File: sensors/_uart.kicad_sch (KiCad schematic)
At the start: 19 parts, among them J5 JP_GPS, J6 JP_RADIO, U1 SC16IS752IPW

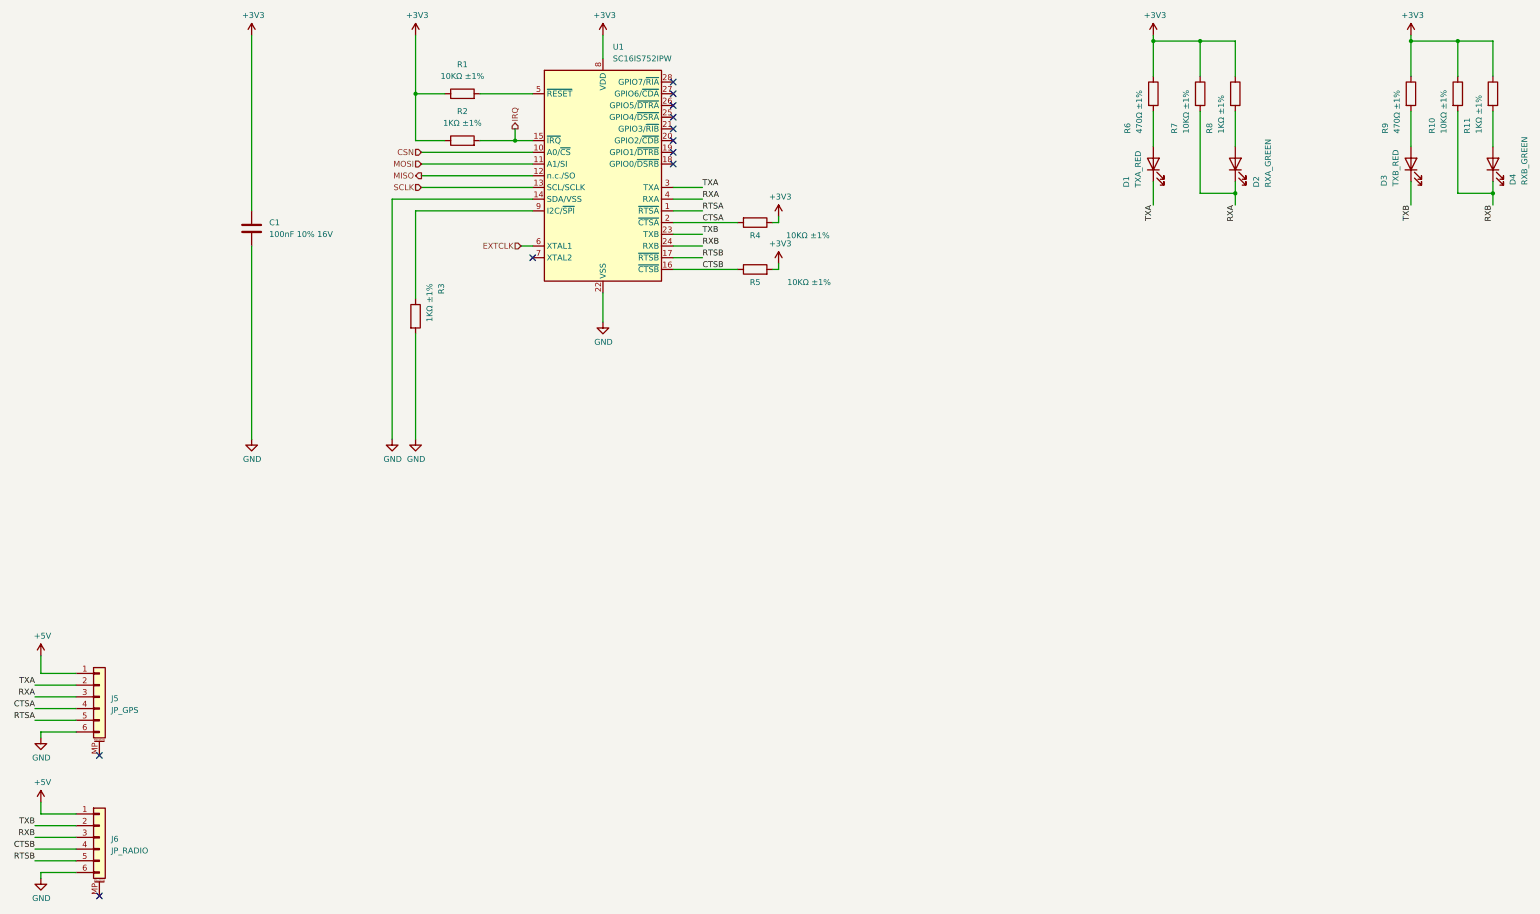
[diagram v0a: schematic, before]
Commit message: changes from dshot branch
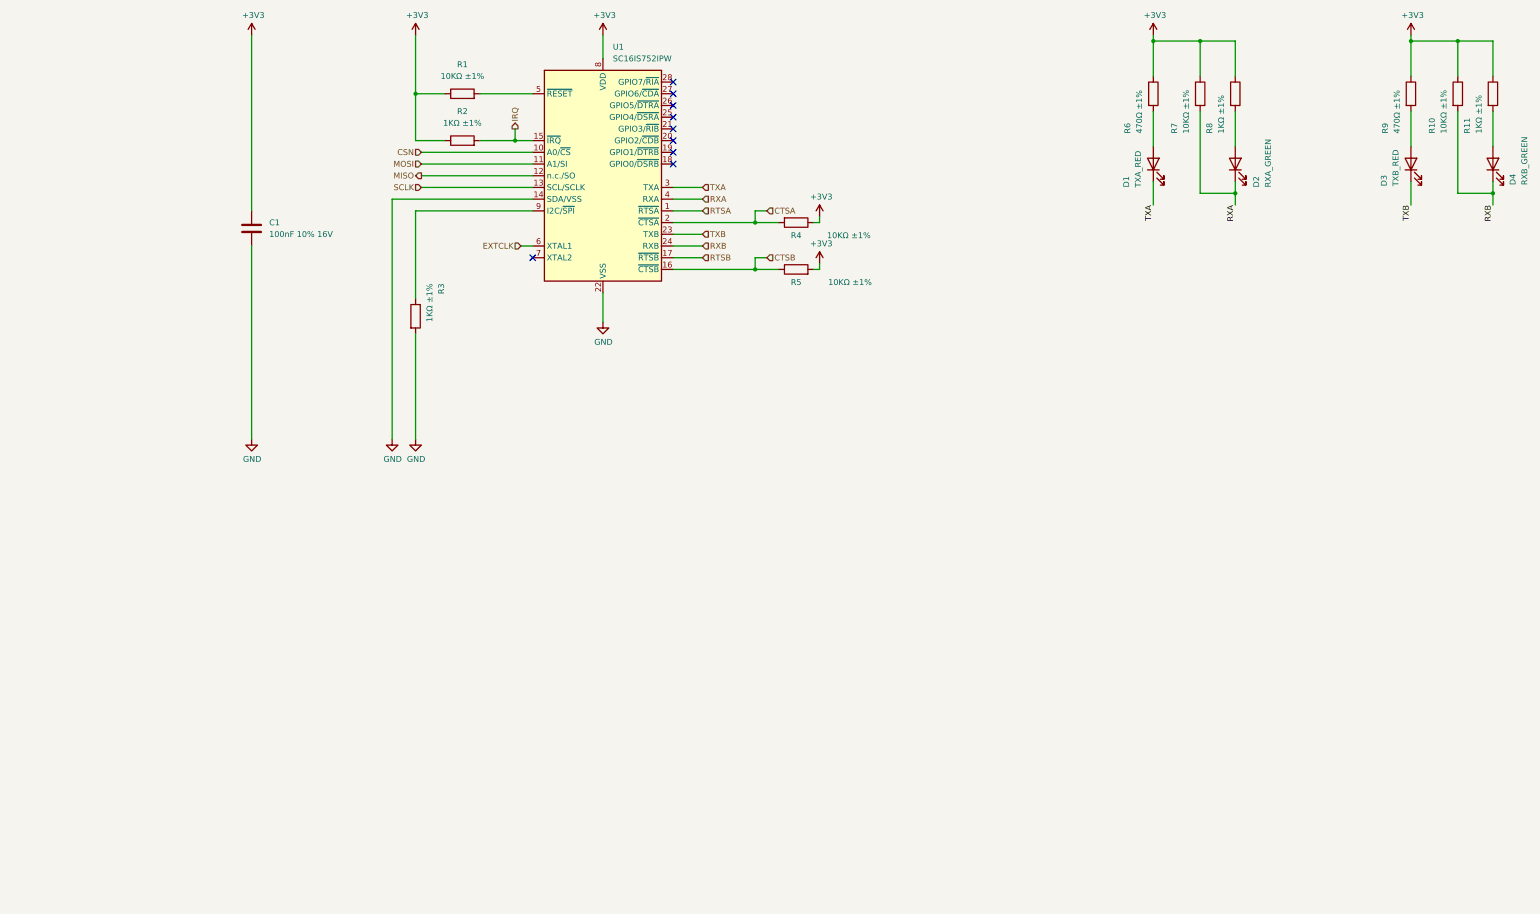
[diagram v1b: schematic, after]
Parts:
- removed J5: JP_GPS, Connector_Molex:Molex_PicoBlade_53261-0671_1x06-1MP_P1.25mm_Horizontal, symbol Connector_Generic_MountingPin:Conn_01x06_MountingPin
- removed J6: JP_RADIO, Connector_Molex:Molex_PicoBlade_53261-0671_1x06-1MP_P1.25mm_Horizontal, symbol Connector_Generic_MountingPin:Conn_01x06_MountingPin
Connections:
- no-connect marks 11 -> 9
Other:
- moved on the sheet: R4, R5

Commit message: replace MS561101 pressure sensor with SPL06-001
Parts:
- C1: Part CC0402X7R50V104KN -> CL05B104KB54PNC
- R11, R2, R3, R8: Part SCR0402F1K -> 0402WGF1001TCE
- R6, R9: Part FRC0402F4700TS -> 0402WGF4700TCE
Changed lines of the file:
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@@
 			)
 		)
-		(property "Part" "FRC0402F4700TS"
+		(property "Part" "0402WGF4700TCE"
 			(at 271.78 81.28 0)
 			(hide yes)
@@
 			)
 		)
-		(property "Part" "SCR0402F1K"
+		(property "Part" "0402WGF1001TCE"
 			(at 121.92 91.44 0)
 			(hide yes)
@@
 			)
 		)
-		(property "Part" "SCR0402F1K"
+		(property "Part" "0402WGF1001TCE"
 			(at 111.76 129.54 0)
 			(hide yes)
@@
 			)
 		)
-		(property "Part" "CC0402X7R50V104KN"
+		(property "Part" "CL05B104KB54PNC"
 			(at 76.2 110.49 0)
 			(hide yes)
@@
 			)
 		)
-		(property "Part" "SCR0402F1K"
+		(property "Part" "0402WGF1001TCE"
 			(at 345.44 81.28 0)
 			(hide yes)
@@
 			)
 		)
-		(property "Part" "SCR0402F1K"
+		(property "Part" "0402WGF1001TCE"
 			(at 289.56 81.28 0)
 			(hide yes)
@@
 			)
 		)
-		(property "Part" "FRC0402F4700TS"
+		(property "Part" "0402WGF4700TCE"
 			(at 327.66 81.28 0)
 			(hide yes)

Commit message: move SP3485 to sensors board and connect to UART port A
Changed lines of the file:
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@@
 	)
 	(hierarchical_label "RTSA"
-		(shape input)
+		(shape output)
 		(at 173.99 106.68 0)
 		(effects
@@
 	)
 	(hierarchical_label "RTSB"
-		(shape input)
+		(shape output)
 		(at 173.99 116.84 0)
 		(effects
@@
 	)
 	(hierarchical_label "TXA"
-		(shape input)
+		(shape output)
 		(at 173.99 101.6 0)
 		(effects
@@
 	)
 	(hierarchical_label "TXB"
-		(shape input)
+		(shape output)
 		(at 173.99 111.76 0)
 		(effects

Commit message: use series resistor for external clk; add 1uF caps
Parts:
- added C19: 1uF (105) 10% 50V, Capacitor_SMD:C_0603_1608Metric, symbol Device:C
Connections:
- net +3V3: now also C19.1
- net GND: now also C19.2
